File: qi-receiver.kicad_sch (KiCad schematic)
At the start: 39 parts, among them J104 LiPo BATTERY, Q101 IRF7606TRPBF, Q107 IRF7606TRPBF, Q108 IRF7606TRPBF, U101 BQ51013BRHLR, U104 MCP73831-2-OT, U401 LD1117S33TR_SOT223

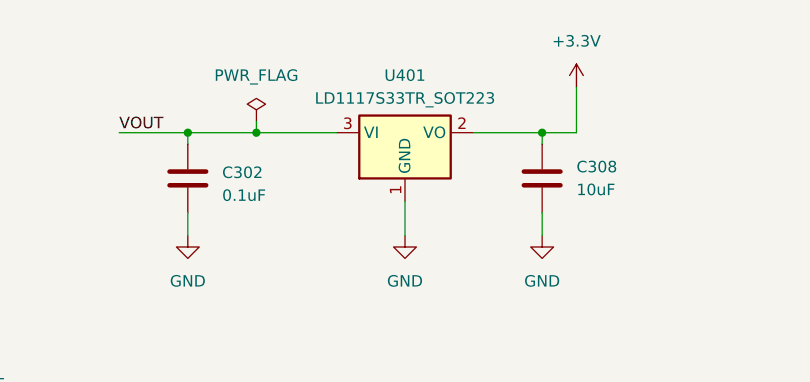
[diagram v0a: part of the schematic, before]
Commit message: Change Regulator IC and Pullup R
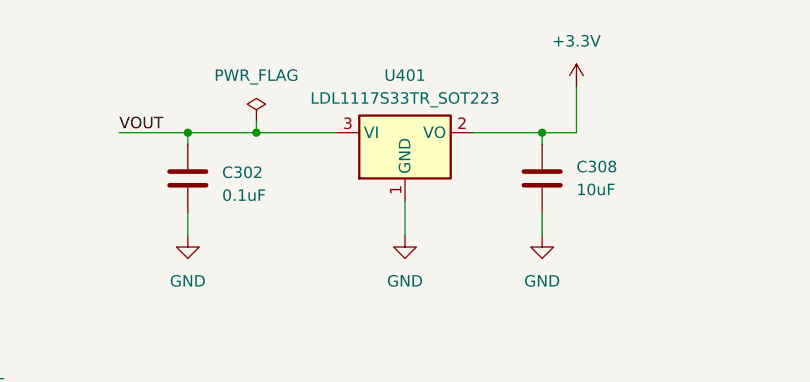
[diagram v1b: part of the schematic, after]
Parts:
- R304: digikey 311-100KGRCT-ND -> 13-RC0603JR-1010KLCT-ND
- U401: value LD1117S33TR_SOT223 -> LDL1117S33TR_SOT223
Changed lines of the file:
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@@
 			)
 		)
-		(property "digikey" "311-100KGRCT-ND"
+		(property "digikey" "13-RC0603JR-1010KLCT-ND"
 			(at 238.76 110.49 0)
 			(effects
@@
 			)
 		)
-		(property "Value" "LD1117S33TR_SOT223"
+		(property "Value" "LDL1117S33TR_SOT223"
 			(at 139.7 33.02 0)
 			(effects
